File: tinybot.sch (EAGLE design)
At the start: 18 parts, among them Q1 MOSFET-PCHANNEL, Q2 2N7002PW, Q3 2N7002PW, U1 MCP73831, U2 TINY85-20-DIP

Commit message: fixed motor mosfet wiring (again)
Still had it wrong!  Motor mosfets connected to 5V (from USB), not VCC.
Now fixed.

Also added logo/name/url to bottom silk!
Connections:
- net 5V: no longer LMOT1+.P, RMOT+.P
- net VCC: now also LMOT1+.P, RMOT+.P
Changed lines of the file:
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@@
 <part name="GND12" library="SparkFun-Aesthetics" deviceset="GND" device=""/>
 <part name="C2" library="rcl" deviceset="C-US" device="025-025X050" value="1 uf"/>
-<part name="SUPPLY5" library="SparkFun-Aesthetics" deviceset="5V" device=""/>
-<part name="SUPPLY6" library="SparkFun-Aesthetics" deviceset="5V" device=""/>
 </parts>
 <sheets>
@@
 <attribute name="VALUE" x="-69.469" y="-21.59" size="1.778" layer="96"/>
 </instance>
-<instance part="SUPPLY5" gate="G$1" x="27.94" y="-25.4"/>
-<instance part="SUPPLY6" gate="G$1" x="50.8" y="-25.4"/>
 </instances>
 <busses>
@@
 </segment>
 <segment>
-<pinref part="JP1" gate="G$1" pin="VBUS"/>
-<wire x1="-106.68" y1="5.08" x2="-96.52" y2="5.08" width="0.1524" layer="91"/>
-<wire x1="-96.52" y1="5.08" x2="-96.52" y2="17.78" width="0.1524" layer="91"/>
-<pinref part="SUPPLY1" gate="G$1" pin="5V"/>
-<wire x1="-96.52" y1="5.08" x2="-96.52" y2="-5.08" width="0.1524" layer="91"/>
-<pinref part="R1" gate="G$1" pin="2"/>
-<junction x="-96.52" y="5.08"/>
-</segment>
-<segment>
 <pinref part="Q1" gate="G$1" pin="G"/>
 <wire x1="-71.12" y1="0" x2="-71.12" y2="17.78" width="0.1524" layer="91"/>
@@
 </segment>
 <segment>
-<pinref part="LMOT1+" gate="G$1" pin="P"/>
-<wire x1="38.1" y1="-55.88" x2="27.94" y2="-55.88" width="0.1524" layer="91"/>
-<wire x1="27.94" y1="-55.88" x2="27.94" y2="-25.4" width="0.1524" layer="91"/>
-<pinref part="SUPPLY5" gate="G$1" pin="5V"/>
-</segment>
-<segment>
-<pinref part="RMOT+" gate="G$1" pin="P"/>
-<wire x1="58.42" y1="-55.88" x2="50.8" y2="-55.88" width="0.1524" layer="91"/>
-<wire x1="50.8" y1="-55.88" x2="50.8" y2="-25.4" width="0.1524" layer="91"/>
-<pinref part="SUPPLY6" gate="G$1" pin="5V"/>
+<pinref part="SUPPLY1" gate="G$1" pin="5V"/>
+<wire x1="-96.52" y1="17.78" x2="-96.52" y2="5.08" width="0.1524" layer="91"/>
+<pinref part="JP1" gate="G$1" pin="VBUS"/>
+<wire x1="-96.52" y1="5.08" x2="-106.68" y2="5.08" width="0.1524" layer="91"/>
+<pinref part="R1" gate="G$1" pin="2"/>
+<wire x1="-96.52" y1="-5.08" x2="-96.52" y2="5.08" width="0.1524" layer="91"/>
+<junction x="-96.52" y="5.08"/>
 </segment>
 </net>
@@
 <pinref part="C2" gate="G$1" pin="2"/>
 <wire x1="-67.31" y1="-19.05" x2="-63.5" y2="-19.05" width="0.1524" layer="91"/>
-<wire x1="-63.5" y1="-19.05" x2="-63.5" y2="-48.26" width="0.1524" layer="91"/>
+<wire x1="-63.5" y1="-19.05" x2="-63.5" y2="-33.02" width="0.1524" layer="91"/>
 <pinref part="U2" gate="G$1" pin="VCC"/>
+<wire x1="-63.5" y1="-33.02" x2="-63.5" y2="-48.26" width="0.1524" layer="91"/>
 <wire x1="-63.5" y1="-48.26" x2="-55.88" y2="-48.26" width="0.1524" layer="91"/>
 <pinref part="Q1" gate="G$1" pin="D"/>
@@
 <wire x1="-63.5" y1="-7.62" x2="-63.5" y2="-19.05" width="0.1524" layer="91"/>
 <junction x="-63.5" y="-19.05"/>
+<pinref part="LMOT1+" gate="G$1" pin="P"/>
+<wire x1="38.1" y1="-55.88" x2="27.94" y2="-55.88" width="0.1524" layer="91"/>
+<wire x1="27.94" y1="-55.88" x2="27.94" y2="-33.02" width="0.1524" layer="91"/>
+<wire x1="27.94" y1="-33.02" x2="-63.5" y2="-33.02" width="0.1524" layer="91"/>
+<junction x="-63.5" y="-33.02"/>
+<pinref part="RMOT+" gate="G$1" pin="P"/>
+<wire x1="58.42" y1="-55.88" x2="50.8" y2="-55.88" width="0.1524" layer="91"/>
+<wire x1="50.8" y1="-55.88" x2="50.8" y2="-33.02" width="0.1524" layer="91"/>
+<wire x1="50.8" y1="-33.02" x2="27.94" y2="-33.02" width="0.1524" layer="91"/>
+<junction x="27.94" y="-33.02"/>
 </segment>
 </net>
@@
 </sheet>
 </sheets>
-<errors>
-</errors>
 </schematic>
 </drawing>

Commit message: Decreased charge current from 500mA to 100mA
R3 changed from 2K to 10K
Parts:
- R3: value 2K -> 10K
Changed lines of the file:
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@@
 <part name="GND11" library="SparkFun-Aesthetics" deviceset="GND" device=""/>
 <part name="SUPPLY3" library="SparkFun-Aesthetics" deviceset="5V" device=""/>
-<part name="R3" library="rcl" deviceset="R-US_" device="0204/5" value="2K"/>
+<part name="R3" library="rcl" deviceset="R-US_" device="0204/5" value="10K"/>
 <part name="GND4" library="SparkFun-Aesthetics" deviceset="GND" device=""/>
 <part name="C1" library="rcl" deviceset="C-US" device="025-025X050" value="4.7 uf"/>

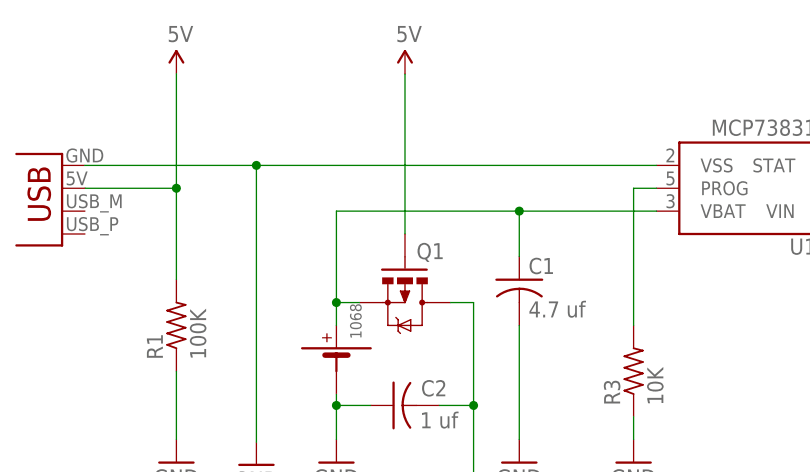
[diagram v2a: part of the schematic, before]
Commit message: improved mosfet pad layout and corrected battery holder hole size
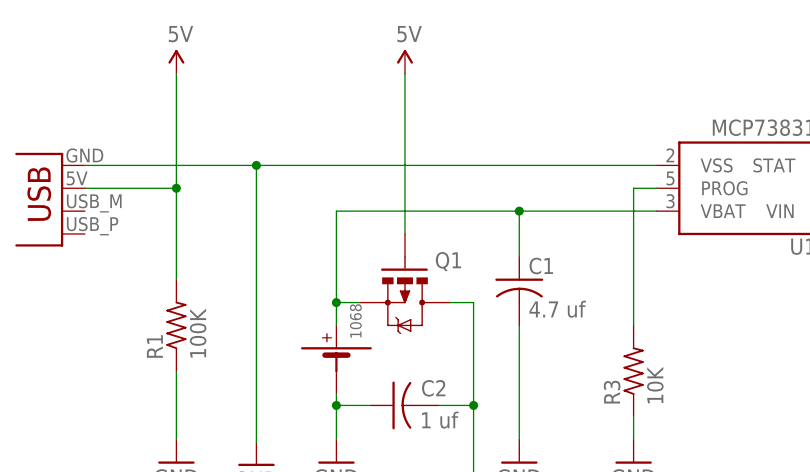
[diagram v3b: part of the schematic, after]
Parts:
- Q2, Q3: device SparkFun-DiscreteSemi:MOSFET-NCHANNEL2N7002PW -> SparkFun-DiscreteSemi:MOSFET-NCHANNELBSS138
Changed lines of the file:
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@@
 <layer number="1" name="Top" color="4" fill="1" visible="no" active="no"/>
 <layer number="16" name="Bottom" color="1" fill="1" visible="no" active="no"/>
-<layer number="17" name="Pads" color="2" fill="1" visible="no" active="no"/>
-<layer number="18" name="Vias" color="2" fill="1" visible="no" active="no"/>
+<layer number="17" name="Pads" color="10" fill="1" visible="no" active="no"/>
+<layer number="18" name="Vias" color="10" fill="1" visible="no" active="no"/>
 <layer number="19" name="Unrouted" color="6" fill="1" visible="no" active="no"/>
 <layer number="20" name="Dimension" color="15" fill="1" visible="no" active="no"/>
-<layer number="21" name="tPlace" color="16" fill="1" visible="no" active="no"/>
+<layer number="21" name="tPlace" color="15" fill="1" visible="no" active="no"/>
 <layer number="22" name="bPlace" color="7" fill="1" visible="no" active="no"/>
 <layer number="23" name="tOrigins" color="15" fill="1" visible="no" active="no"/>
 <layer number="24" name="bOrigins" color="15" fill="1" visible="no" active="no"/>
-<layer number="25" name="tNames" color="7" fill="1" visible="no" active="no"/>
+<layer number="25" name="tNames" color="16" fill="1" visible="no" active="no"/>
 <layer number="26" name="bNames" color="7" fill="1" visible="no" active="no"/>
 <layer number="27" name="tValues" color="7" fill="1" visible="no" active="no"/>
@@
 <layer number="50" name="dxf" color="7" fill="1" visible="no" active="no"/>
 <layer number="51" name="tDocu" color="14" fill="1" visible="no" active="no"/>
-<layer number="52" name="bDocu" color="7" fill="1" visible="no" active="no"/>
+<layer number="52" name="bDocu" color="14" fill="1" visible="no" active="no"/>
 <layer number="53" name="tGND_GNDA" color="7" fill="9" visible="no" active="no"/>
 <layer number="54" name="bGND_GNDA" color="1" fill="9" visible="no" active="no"/>
@@
 <part name="U2" library="SparkFun-DigitalIC" deviceset="ATTINY45" device="TINY85-20-DIP" value="TINY85-20-DIP"/>
 <part name="GND5" library="SparkFun-Aesthetics" deviceset="GND" device=""/>
-<part name="Q3" library="SparkFun-DiscreteSemi" deviceset="MOSFET-NCHANNEL" device="2N7002PW" value="2N7002PW"/>
-<part name="Q2" library="SparkFun-DiscreteSemi" deviceset="MOSFET-NCHANNEL" device="2N7002PW" value="2N7002PW"/>
+<part name="Q3" library="SparkFun-DiscreteSemi" deviceset="MOSFET-NCHANNEL" device="BSS138" value="2N7002PW"/>
+<part name="Q2" library="SparkFun-DiscreteSemi" deviceset="MOSFET-NCHANNEL" device="BSS138" value="2N7002PW"/>
 <part name="GND6" library="SparkFun-Aesthetics" deviceset="GND" device=""/>
 <part name="GND7" library="SparkFun-Aesthetics" deviceset="GND" device=""/>
@@
 <part name="RMOT+" library="wirepad" deviceset="WIREPAD" device="SMD1,27-254"/>
 <part name="U$1" library="keystone" deviceset="1068" device=""/>
-<part name="Q1" library="SparkFun-DiscreteSemi" deviceset="MOSFET-PCHANNEL" device=""/>
 <part name="R1" library="rcl" deviceset="R-US_" device="0204/5" value="100K"/>
 <part name="GND10" library="SparkFun-Aesthetics" deviceset="GND" device=""/>
@@
 <part name="GND12" library="SparkFun-Aesthetics" deviceset="GND" device=""/>
 <part name="C2" library="rcl" deviceset="C-US" device="025-025X050" value="1 uf"/>
+<part name="Q1" library="SparkFun-DiscreteSemi" deviceset="MOSFET-PCHANNEL" device=""/>
 </parts>
 <sheets>
@@
 <attribute name="VALUE" x="-75.946" y="-11.684" size="1.27" layer="96" rot="R90"/>
 </instance>
-<instance part="Q1" gate="G$1" x="-71.12" y="-7.62" smashed="yes" rot="R270">
-<attribute name="NAME" x="-69.85" y="-2.794" size="1.778" layer="95"/>
-</instance>
 <instance part="R1" gate="G$1" x="-96.52" y="-10.16" rot="R90"/>
 <instance part="GND10" gate="1" x="-78.74" y="-25.4"/>
@@
 <attribute name="VALUE" x="-69.469" y="-21.59" size="1.778" layer="96"/>
 </instance>
+<instance part="Q1" gate="G$1" x="-71.12" y="-7.62" smashed="yes" rot="R270">
+<attribute name="NAME" x="-67.818" y="-3.81" size="1.778" layer="95"/>
+</instance>
 </instances>
 <busses>
@@
 </segment>
 <segment>
-<pinref part="Q1" gate="G$1" pin="G"/>
-<wire x1="-71.12" y1="0" x2="-71.12" y2="17.78" width="0.1524" layer="91"/>
-<pinref part="SUPPLY3" gate="G$1" pin="5V"/>
-</segment>
-<segment>
 <pinref part="SUPPLY1" gate="G$1" pin="5V"/>
 <wire x1="-96.52" y1="17.78" x2="-96.52" y2="5.08" width="0.1524" layer="91"/>
@@
 <junction x="-96.52" y="5.08"/>
 </segment>
+<segment>
+<pinref part="SUPPLY3" gate="G$1" pin="5V"/>
+<pinref part="Q1" gate="G$1" pin="G"/>
+<wire x1="-71.12" y1="17.78" x2="-71.12" y2="0" width="0.1524" layer="91"/>
+</segment>
 </net>
 <net name="N$1" class="0">
@@
 <wire x1="-58.42" y1="2.54" x2="-78.74" y2="2.54" width="0.1524" layer="91"/>
 <wire x1="-78.74" y1="-10.16" x2="-78.74" y2="-7.62" width="0.1524" layer="91"/>
-<pinref part="Q1" gate="G$1" pin="S"/>
+<pinref part="C1" gate="G$1" pin="1"/>
 <wire x1="-78.74" y1="-7.62" x2="-78.74" y2="2.54" width="0.1524" layer="91"/>
-<wire x1="-76.2" y1="-7.62" x2="-78.74" y2="-7.62" width="0.1524" layer="91"/>
-<junction x="-78.74" y="-7.62"/>
-<pinref part="C1" gate="G$1" pin="1"/>
 <wire x1="-58.42" y1="2.54" x2="-58.42" y2="-2.54" width="0.1524" layer="91"/>
 <junction x="-58.42" y="2.54"/>
-</segment>
-</net>
-<net name="N$4" class="0">
-<segment>
-<pinref part="U2" gate="G$1" pin="PB0(MOSI)"/>
-<pinref part="Q3" gate="G$1" pin="G"/>
-<wire x1="-27.94" y1="-48.26" x2="7.62" y2="-48.26" width="0.1524" layer="91"/>
+<junction x="-78.74" y="-7.62"/>
+<pinref part="Q1" gate="G$1" pin="S"/>
+<wire x1="-78.74" y1="-7.62" x2="-76.2" y2="-7.62" width="0.1524" layer="91"/>
 </segment>
 </net>
@@
 <wire x1="-63.5" y1="-33.02" x2="-63.5" y2="-48.26" width="0.1524" layer="91"/>
 <wire x1="-63.5" y1="-48.26" x2="-55.88" y2="-48.26" width="0.1524" layer="91"/>
-<pinref part="Q1" gate="G$1" pin="D"/>
-<wire x1="-66.04" y1="-7.62" x2="-63.5" y2="-7.62" width="0.1524" layer="91"/>
 <wire x1="-63.5" y1="-7.62" x2="-63.5" y2="-19.05" width="0.1524" layer="91"/>
 <junction x="-63.5" y="-19.05"/>
@@
 <wire x1="50.8" y1="-33.02" x2="27.94" y2="-33.02" width="0.1524" layer="91"/>
 <junction x="27.94" y="-33.02"/>
+<pinref part="Q1" gate="G$1" pin="D"/>
+<wire x1="-63.5" y1="-7.62" x2="-66.04" y2="-7.62" width="0.1524" layer="91"/>
 </segment>
 </net>
@@
 </segment>
 </net>
+<net name="N$4" class="0">
+<segment>
+<pinref part="U2" gate="G$1" pin="PB0(MOSI)"/>
+<pinref part="Q3" gate="G$1" pin="G"/>
+<wire x1="-27.94" y1="-48.26" x2="7.62" y2="-48.26" width="0.1524" layer="91"/>
+</segment>
+</net>
